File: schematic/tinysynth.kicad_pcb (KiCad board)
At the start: 2 copper layers, 43.5 x 21 mm, 11 parts, among them CN1 NMJ6HCD2, U1 ATtiny85-20S, U2 DIN-504D-M5

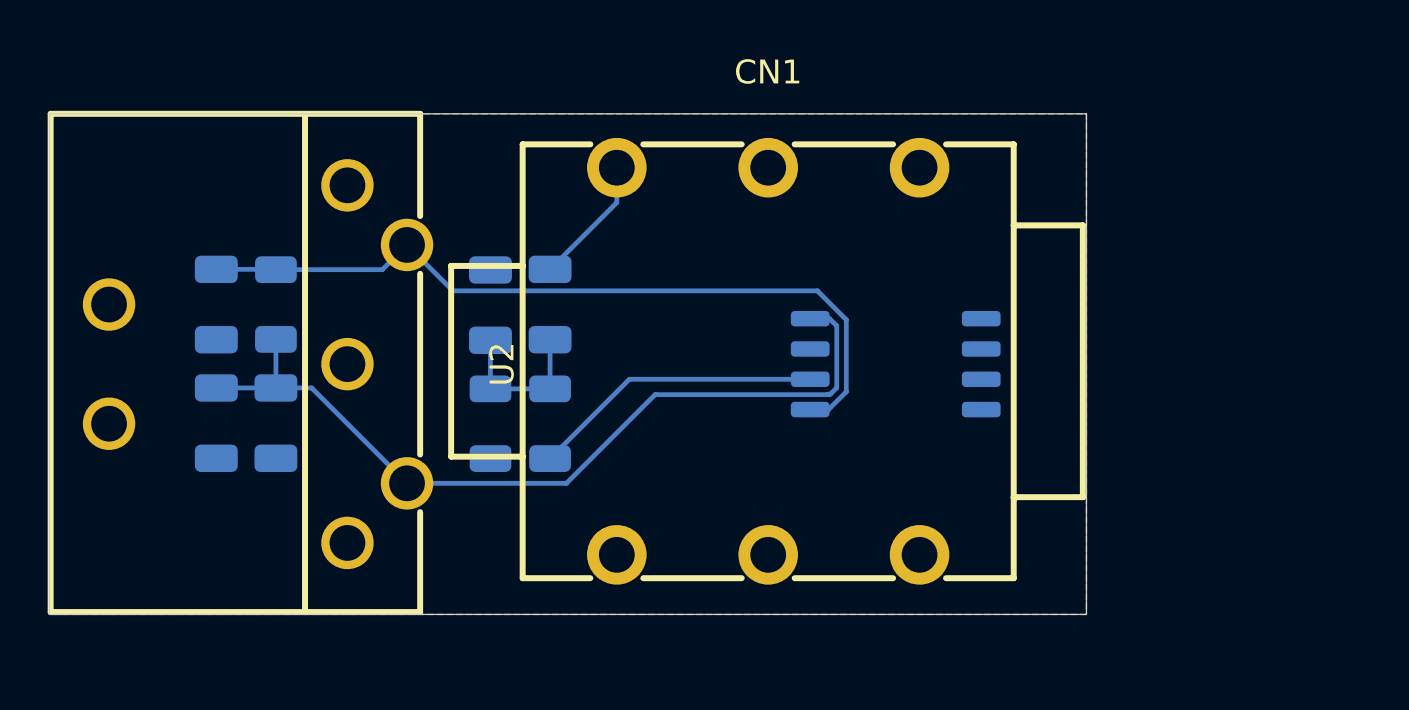
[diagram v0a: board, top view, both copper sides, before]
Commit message: did attiny25 socket version
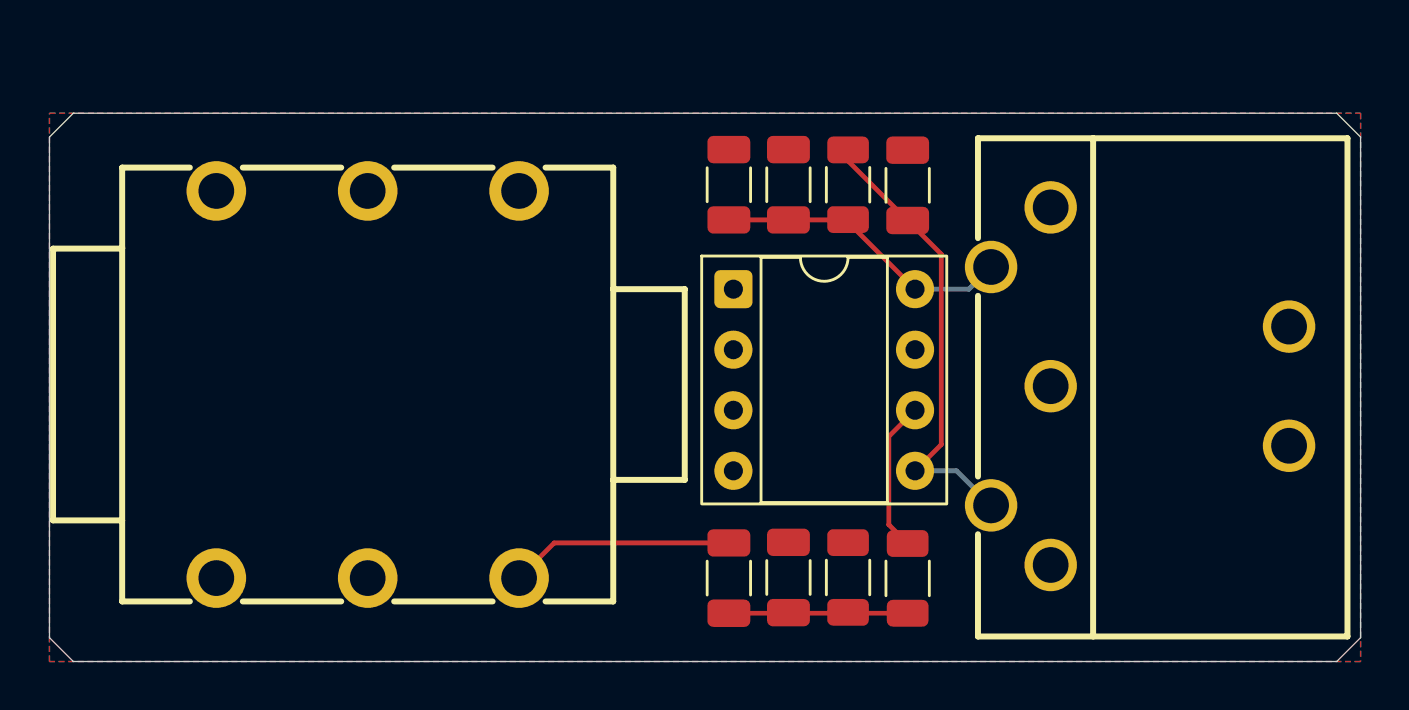
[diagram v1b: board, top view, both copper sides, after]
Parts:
- C1, C2, C3, C4, C5, R1, R2, R3: moved to F.Cu
- U1: value ATtiny85-20S -> ATtiny85-20P; footprint Package_SO:SOIC-8_5.3x5.3mm_P1.27mm -> Package_DIP:DIP-8_W7.62mm_Socket; moved to F.Cu
- moved U2 37.0 mm to (60.8, 26.4), turned to 90 degrees
- moved C4 29.4 mm to (51.0, 18.0), turned to 90 degrees
- moved R1 24.5 mm to (48.5, 18.0)
- moved C1 23.7 mm to (43.5, 18.0), turned to 90 degrees
- moved C2 23.7 mm to (46.0, 18.0), turned to 90 degrees
- moved C3 16.9 mm to (46.0, 34.5)
- moved CN1 16.8 mm to (28.4, 26.4), turned to 180 degrees
- moved R2 16.3 mm to (51.0, 34.5), turned to 90 degrees
- moved R3 16.3 mm to (48.5, 34.5), turned to 90 degrees
- moved C5 13.7 mm to (43.5, 34.5)
- moved U1 7.50 mm to (43.7, 22.4), turned to 0 degrees
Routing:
- net Net-(U1-VCC): track 35.2 -> 12.6 mm
- net Net-(U1-AREF/PB0): track 33.0 -> 19.3 mm
- net Net-(U1-PB1): track 12.3 -> 6.37 mm
- net Net-(CN1-T): track 5.42 -> 9.41 mm
- net Net-(C3-Pad1): track 6.60 -> 7.50 mm
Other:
- board size 43.5 x 21 mm -> 55 x 23 mm
